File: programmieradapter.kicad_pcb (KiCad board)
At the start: 2 copper layers, 57.8 x 50.9 mm, 18 parts, among them SW1 SW_Push

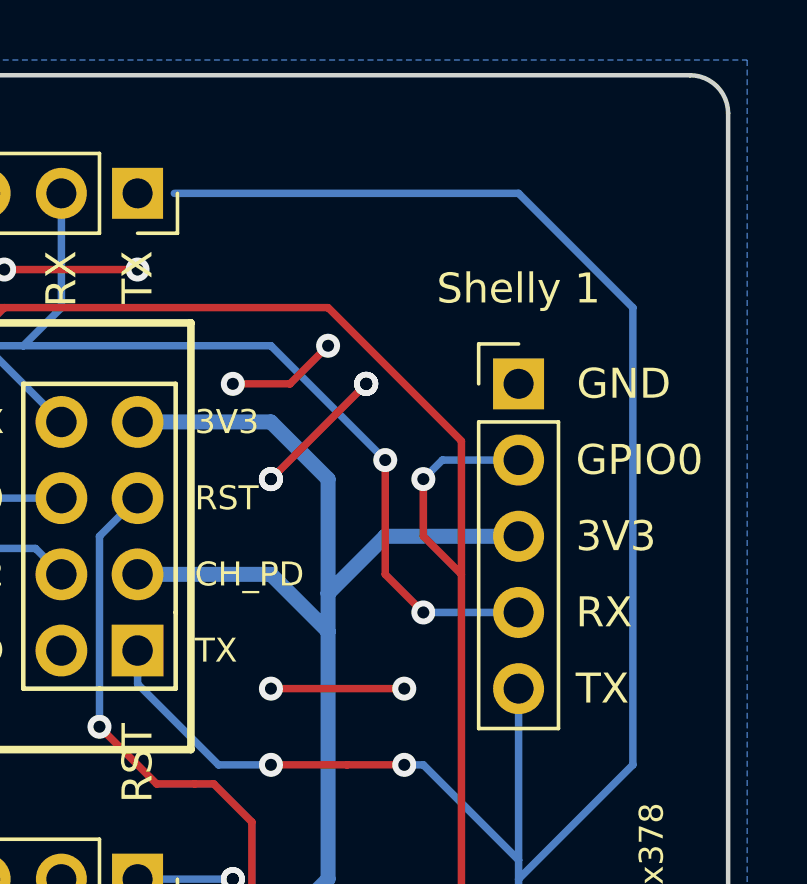
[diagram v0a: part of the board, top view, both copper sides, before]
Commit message: add missing connection to GND for shelly
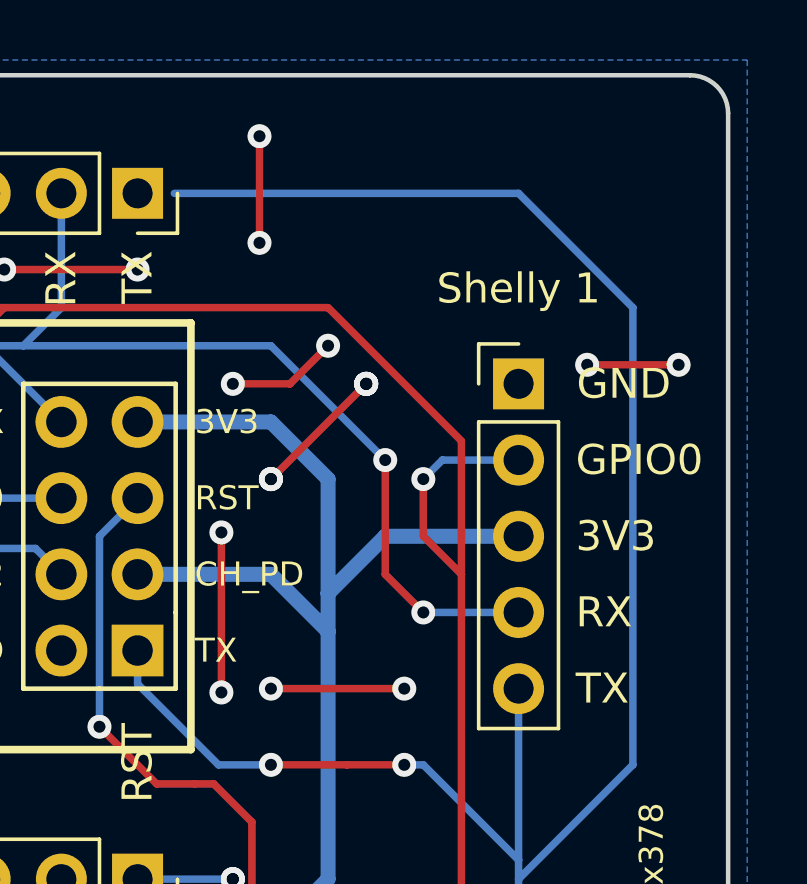
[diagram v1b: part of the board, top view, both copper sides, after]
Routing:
- net GND: track 50.9 -> 62.8 mm, vias 24 -> 30
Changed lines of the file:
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@@
     (thickness 1.6)
     (drawings 39)
-    (tracks 282)
+    (tracks 291)
     (zones 0)
     (modules 18)
@@
   (via (at 57.15 29.845) (size 0.8) (drill 0.4) (layers F.Cu B.Cu) (net 1))
   (segment (start 52.705 29.845) (end 57.15 29.845) (width 0.25) (layer F.Cu) (net 1))
+  (via (at 75.184 33.02) (size 0.8) (drill 0.4) (layers F.Cu B.Cu) (net 1))
+  (via (at 72.136 33.02) (size 0.8) (drill 0.4) (layers F.Cu B.Cu) (net 1))
+  (segment (start 72.136 33.02) (end 75.184 33.02) (width 0.25) (layer F.Cu) (net 1))
+  (via (at 61.214 28.956) (size 0.8) (drill 0.4) (layers F.Cu B.Cu) (net 1))
+  (via (at 61.214 25.4) (size 0.8) (drill 0.4) (layers F.Cu B.Cu) (net 1))
+  (via (at 59.944 38.608) (size 0.8) (drill 0.4) (layers F.Cu B.Cu) (net 1))
+  (via (at 59.944 43.942) (size 0.8) (drill 0.4) (layers F.Cu B.Cu) (net 1))
+  (segment (start 59.944 38.608) (end 59.944 43.942) (width 0.25) (layer F.Cu) (net 1))
+  (segment (start 61.214 25.4) (end 61.214 28.956) (width 0.25) (layer F.Cu) (net 1))
   (segment (start 44.958 61.725) (end 44.958 62.865) (width 0.5) (layer F.Cu) (net 2))
   (segment (start 43.307 64.516) (end 43.307 66.675) (width 0.5) (layer F.Cu) (net 2))

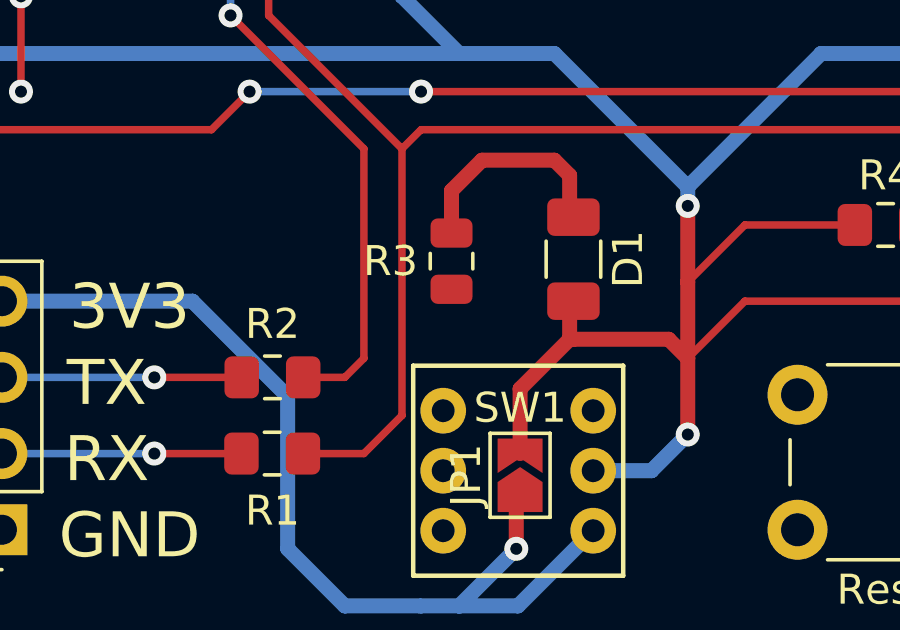
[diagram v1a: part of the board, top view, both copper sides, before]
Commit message: fix an error where the power indication LED did not have connection to GND
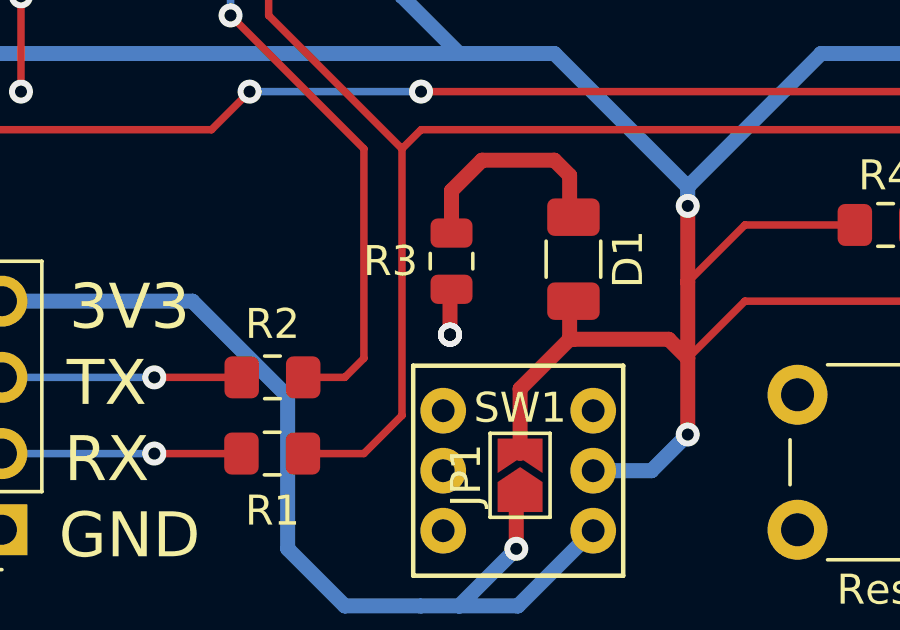
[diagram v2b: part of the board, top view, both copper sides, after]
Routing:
- net GND: track 62.8 -> 64.3 mm, vias 30 -> 33
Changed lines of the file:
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@@
     (thickness 1.6)
     (drawings 39)
-    (tracks 291)
+    (tracks 296)
     (zones 0)
     (modules 18)
@@
   (segment (start 59.944 38.608) (end 59.944 43.942) (width 0.25) (layer F.Cu) (net 1))
   (segment (start 61.214 25.4) (end 61.214 28.956) (width 0.25) (layer F.Cu) (net 1))
+  (via (at 40.9702 62.7126) (size 0.8) (drill 0.4) (layers F.Cu B.Cu) (net 1))
+  (via (at 40.9702 62.7126) (size 0.8) (drill 0.4) (layers F.Cu B.Cu) (net 1))
+  (via (at 40.9702 62.7126) (size 0.8) (drill 0.4) (layers F.Cu B.Cu) (net 1))
+  (segment (start 40.9702 61.2498) (end 41.021 61.199) (width 0.25) (layer F.Cu) (net 1))
+  (segment (start 40.9702 62.7126) (end 40.9702 61.2498) (width 0.5) (layer F.Cu) (net 1))
   (segment (start 44.958 61.725) (end 44.958 62.865) (width 0.5) (layer F.Cu) (net 2))
   (segment (start 43.307 64.516) (end 43.307 66.675) (width 0.5) (layer F.Cu) (net 2))
